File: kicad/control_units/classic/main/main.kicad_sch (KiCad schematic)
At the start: 0 parts

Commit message: Power supply for STM32 for Classic control unit
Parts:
- added C1, C4, C6: 100n, symbol Device:C
- added C2: 10n, symbol Device:C
- added C3: 1u, symbol Device:C
- added C5: 4.7u, symbol Device:C
- added J1: Conn_01x05, symbol Connector_Generic:Conn_01x05
- added J2: USB_C_Receptacle_USB2.0_14P, symbol Connector:USB_C_Receptacle_USB2.0_14P
- added R1, R2: 5.1k, symbol Device:R
- added U1: STM32U031F4Px, Package_SO:TSSOP-20_4.4x6.5mm_P0.65mm, symbol MCU_ST_STM32U0:STM32U031F4Px
- added U2: AZ1117CH2-3.3, Package_TO_SOT_SMD:SOT-223-3_TabPin2, symbol Regulator_Linear:AZ1117CH2-3.3
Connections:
- new net: J2.A5 (CC1), R1.1
- new net: J2.B5 (CC2), R2.1
- new net +3V3: C1.1, C2.2, C3.2, C4.1, C5.1, J1.1 (Pin_1), U1.3 (VDD), U1.7 (VDDA), U2.3 (OUT)
- new net +5V: C6.1, J2.A4 (VBUS), J2.A9 (VBUS), J2.B4 (VBUS), J2.B9 (VBUS), U2.1 (IN)
- new net GND: C1.2, C2.1, C3.1, C4.2, C5.2, C6.2, J1.5 (Pin_5), J2.A1 (GND), J2.A12 (GND), J2.B1 (GND), J2.B12 (GND), J2.SH (SHIELD), R1.2, R2.2, U1.2 (VSS), U2.2 (GND)
- new net RS485_A: J1.4 (Pin_4)
- new net RS485_B: J1.3 (Pin_3)
- new net SERIAL_TX: J1.2 (Pin_2)
- no-connect marks 0 -> 4
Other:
- note added: "Connector"
- note added: "Decoupling"
- note added: "Regulator"
- note added: "USB-C"

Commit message: More stuff for Classic control unit
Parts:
- added C7: 10u, symbol Device:C
- added C8: 22u, symbol Device:C
- added J3, J4: Conn_01x05, symbol Connector_Generic:Conn_01x05
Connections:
- net +3V3: now also C8.2, J3.5 (Pin_5), J4.1 (Pin_1)
- net +5V: now also C7.2
- net GND: now also C7.1, C8.1, J3.1 (Pin_1), J4.5 (Pin_5)
- net RS485_A: now also J4.4 (Pin_4)
- net RS485_B: now also J4.3 (Pin_3)
- net SERIAL_TX renamed SERIAL_TX_L
- new net LED_RCLK: J3.2 (Pin_2)
- new net LED_SER: J3.4 (Pin_4)
- new net LED_SRCLK: J3.3 (Pin_3)
- new net SERIAL_TX_R: J4.2 (Pin_2)
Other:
- note added: "Connector to LED board"
- note added: "Connector to XLR5 daughterboard (L)"
- note added: "Connector to XLR5 daughterboard (R)"
- note removed: "Connector"
- moved on the sheet: C1, C6, J1, J2, R1, R2, U2

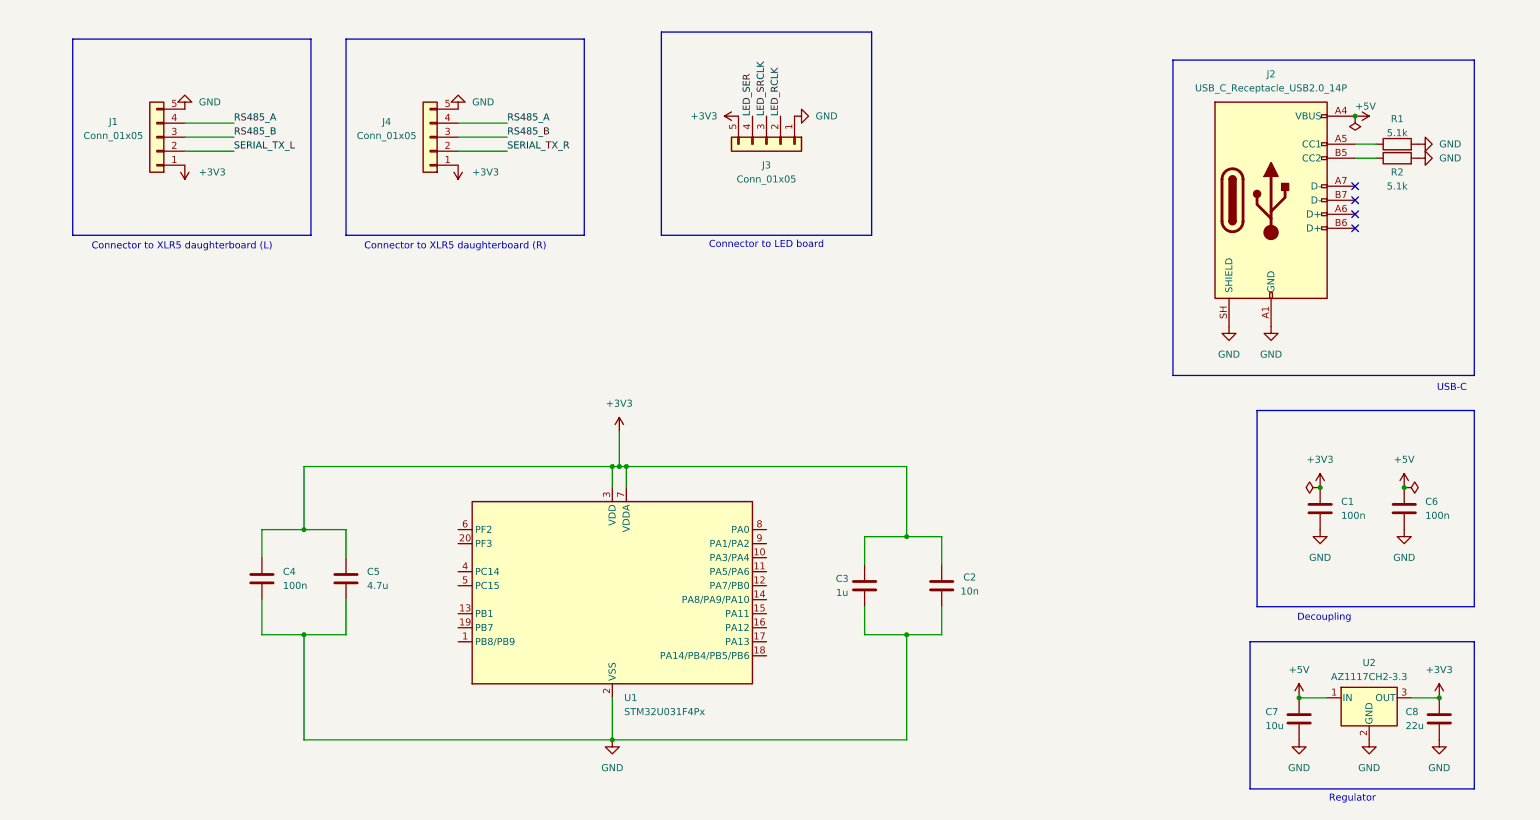
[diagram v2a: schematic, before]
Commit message: fix: Changed Classic control unit MCU and expanded schematic
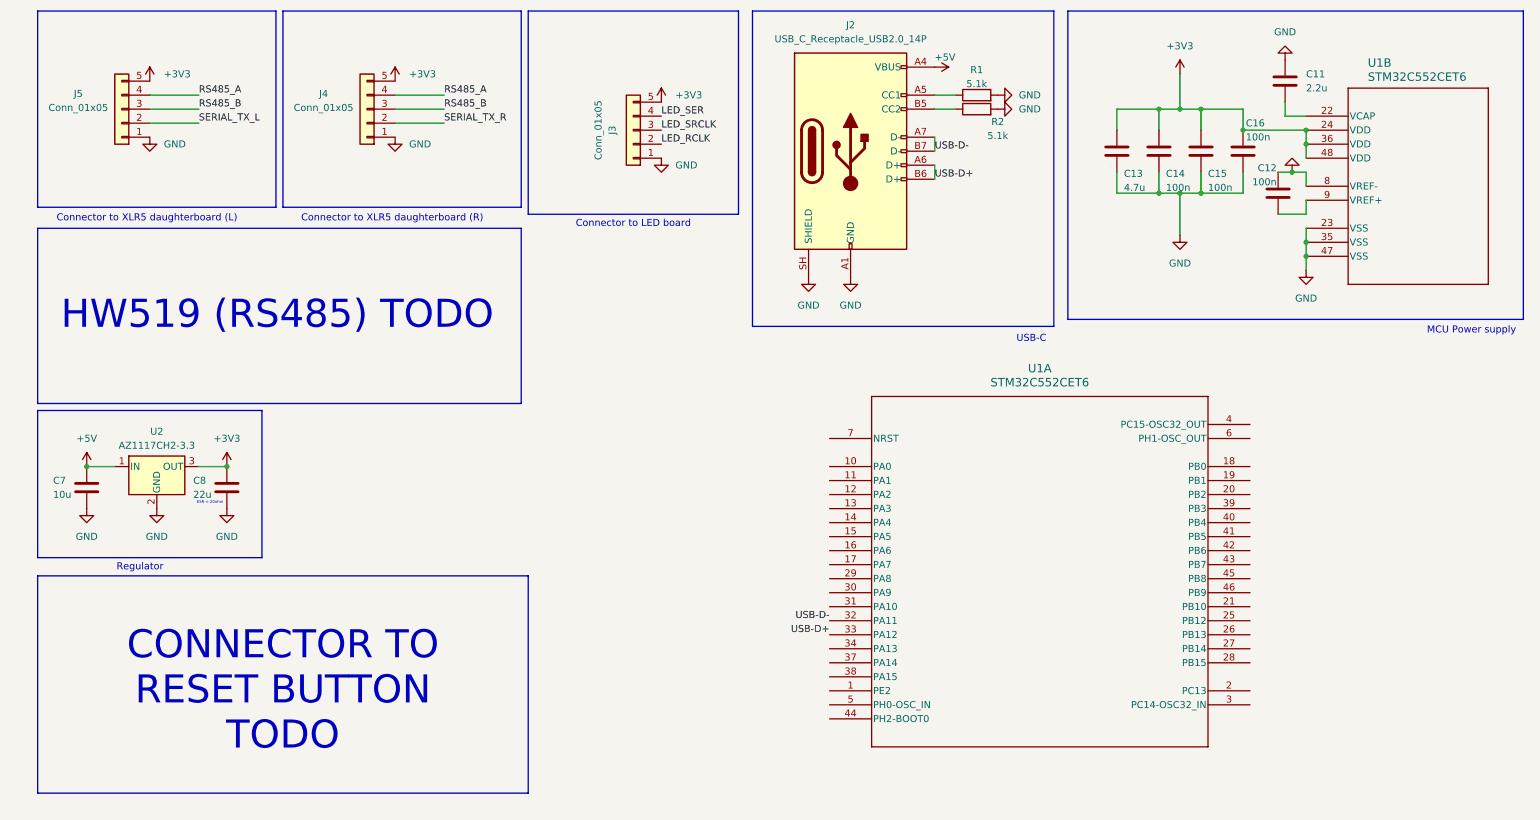
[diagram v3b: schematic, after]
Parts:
- removed C1, C4, C6: 100n, symbol Device:C
- removed C2: 10n, symbol Device:C
- removed C3: 1u, symbol Device:C
- removed C5: 4.7u, symbol Device:C
- removed J1: Conn_01x05, symbol Connector_Generic:Conn_01x05
- removed U1: STM32U031F4Px, Package_SO:TSSOP-20_4.4x6.5mm_P0.65mm, symbol MCU_ST_STM32U0:STM32U031F4Px
- added C11: 2.2u, symbol Device:C
- added C12, C14, C15, C16: 100n, symbol Device:C
- added C13: 4.7u, symbol Device:C
- added J5: Conn_01x05, symbol Connector_Generic:Conn_01x05
- added U1: STM32C552CET6, LQFP-48_STM, symbol STM32C552CET6:STM32C552CET6
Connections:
- net +3V3: now also J4.5 (Pin_5), C13.2, C14.2, C15.2, C16.2, J5.5 (Pin_5), U1.24 (VDD), U1.36 (VDD), U1.48 (VDD); no longer J4.1 (Pin_1)
- net GND: now also J4.1 (Pin_1), C11.1, C12.2, C13.1, C14.1, C15.1, C16.1, J5.1 (Pin_1), U1.23 (VSS), U1.35 (VSS), U1.47 (VSS), U1.8 (VREF-); no longer J4.5 (Pin_5)
- net RS485_A: now also J5.4 (Pin_4)
- net RS485_B: now also J5.3 (Pin_3)
- net SERIAL_TX_L: now also J5.2 (Pin_2)
- net USB-D+: now reaches J2.A6 (D+)
- net USB-D+: now also J2.B6 (D+), U1.33 (PA12)
- net USB-D-: now reaches J2.A7 (D-)
- net USB-D-: now also J2.B7 (D-), U1.32 (PA11)
- new net: C12.1, U1.9 (VREF+)
- new net: C11.2, U1.22 (VCAP)
- no-connect marks 4 -> 0
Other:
- note added: "CONNECTOR TO RESET BUTTON TODO"
- note added: "ESR < 20ohm"
- note added: "HW519 (RS485) TODO"
- note added: "MCU Power supply"
- note removed: "Decoupling"
- moved on the sheet: C7, C8, J2, J3, J4, R1, R2, U2

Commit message: feat: Cleaned up pin arrangement for Classic button/LED assembly, added connector for that on Classic control unit main board, added pins for STM32 TODO
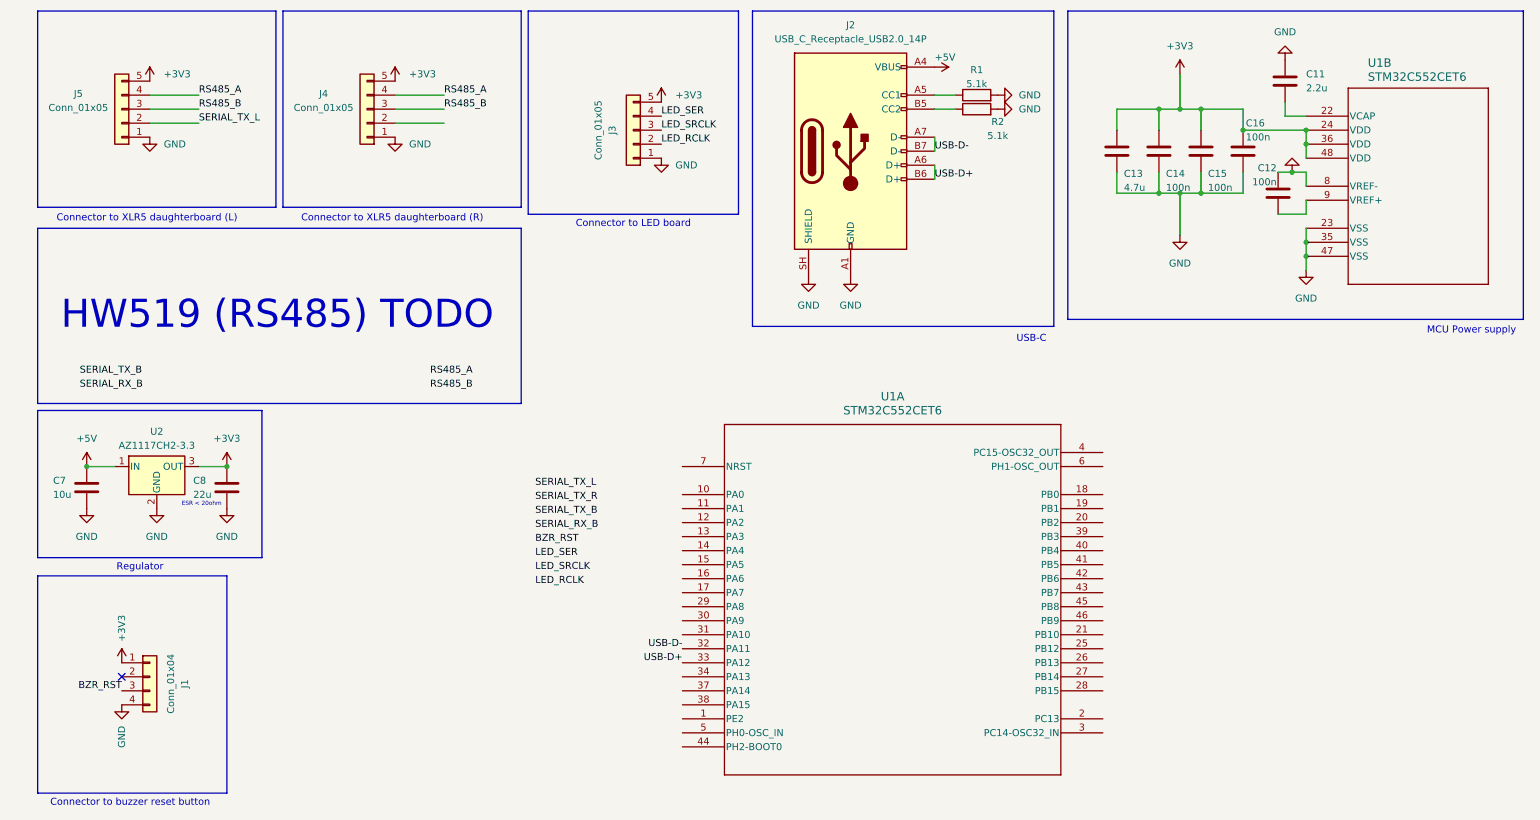
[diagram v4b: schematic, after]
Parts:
- added J1: Conn_01x04, symbol Connector_Generic:Conn_01x04
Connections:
- net +3V3: now also J1.1 (Pin_1)
- net GND: now also J1.4 (Pin_4)
- net SERIAL_TX_R: no longer J4.2 (Pin_2)
- new net BZR_RST: J1.3 (Pin_3)
- no-connect marks 0 -> 1
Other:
- note added: "Connector to buzzer reset button"
- note removed: "CONNECTOR TO RESET BUTTON TODO"
- moved on the sheet: U1A

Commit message: fix: ESD earthing stuff etc. for HW-0519
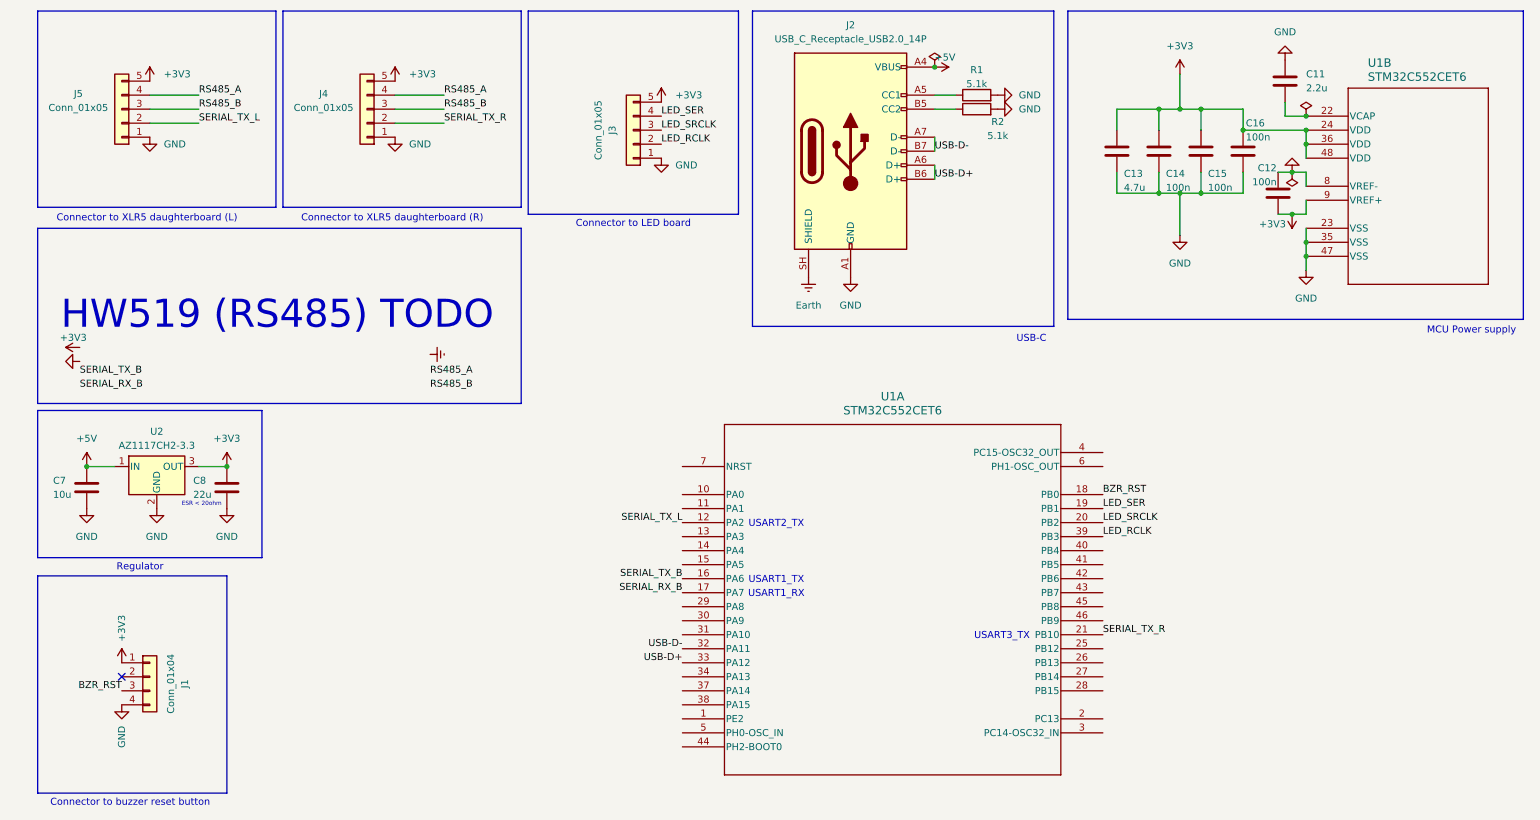
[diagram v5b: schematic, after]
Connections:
- net +3V3: now also C12.1, U1.9 (VREF+)
- net BZR_RST: now also U1.18 (PB0)
- net GND: no longer J2.SH (SHIELD)
- net LED_RCLK: now also U1.39 (PB3)
- net LED_SER: now also U1.19 (PB1)
- net LED_SRCLK: now also U1.20 (PB2)
- net SERIAL_RX_B: now also U1.17 (PA7)
- net SERIAL_TX_B: now also U1.16 (PA6)
- net SERIAL_TX_L: now also U1.12 (PA2)
- net SERIAL_TX_R: now also J4.2 (Pin_2), U1.21 (PB10)
- new net Earth: J2.SH (SHIELD)
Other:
- note added: "USART1_RX"
- note added: "USART1_TX"
- note added: "USART2_TX"
- note added: "USART3_TX"

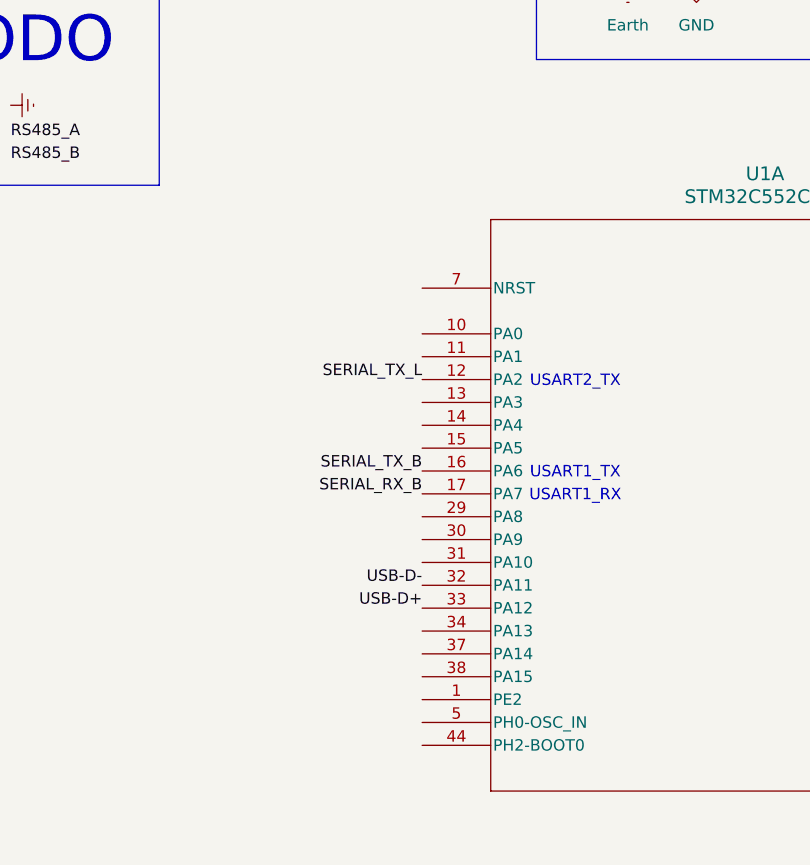
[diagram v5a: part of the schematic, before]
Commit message: feat: Stuff for STM32 programming later
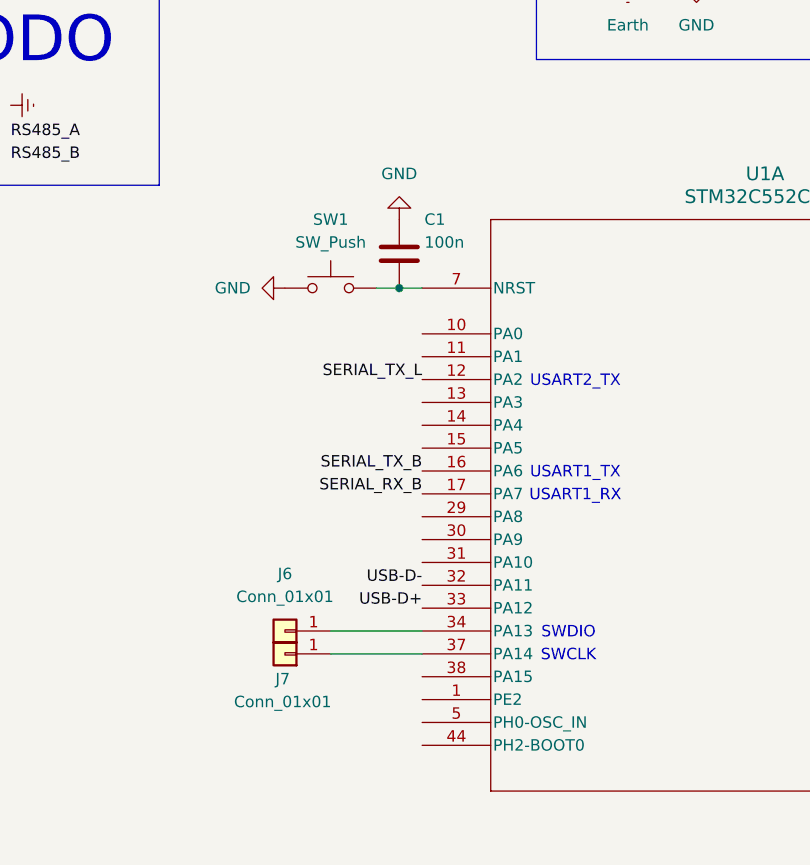
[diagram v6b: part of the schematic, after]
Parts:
- added C1: 100n, symbol Device:C
- added J6, J7: Conn_01x01, symbol Connector_Generic:Conn_01x01
- added SW1: SW_Push, symbol Switch:SW_Push
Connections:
- net GND: now also C1.1, SW1.1
- net at U1.34 (PA13): now also J6.1 (Pin_1)
- net at U1.37 (PA14): now also J7.1 (Pin_1)
- net at U1.7 (NRST): now also C1.2, SW1.2
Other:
- note added: "SWCLK"
- note added: "SWDIO"
